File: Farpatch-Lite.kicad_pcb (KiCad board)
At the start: 2 copper layers, 34 x 12.2 mm, 33 parts, among them J1 Program Header, J2 SWD Connector, SW1 Pushbutton 2.1x1.6mm, SW2 Pushbutton 2.1x1.6mm, U1 ‎ESP32-D0WD-V3‎, U2 Flash 32 Mb SPI, Y1 Crystal 40MHz

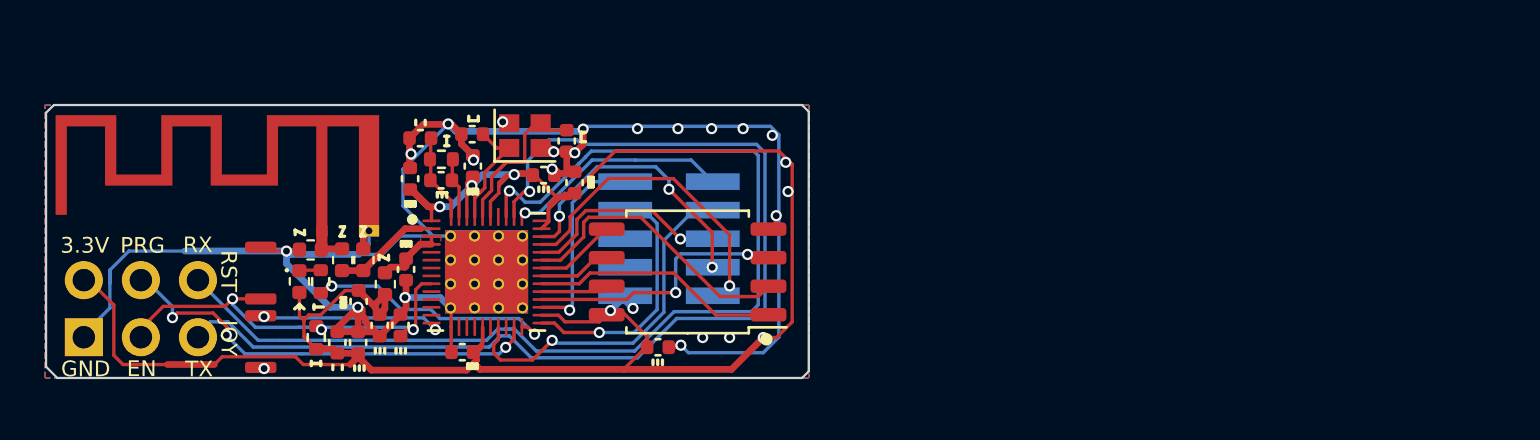
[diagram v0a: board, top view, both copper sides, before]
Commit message: farpatch-lite: Add fabrication data to PCB
Signed-off-by: Sean Cross <sean@xobs.io>
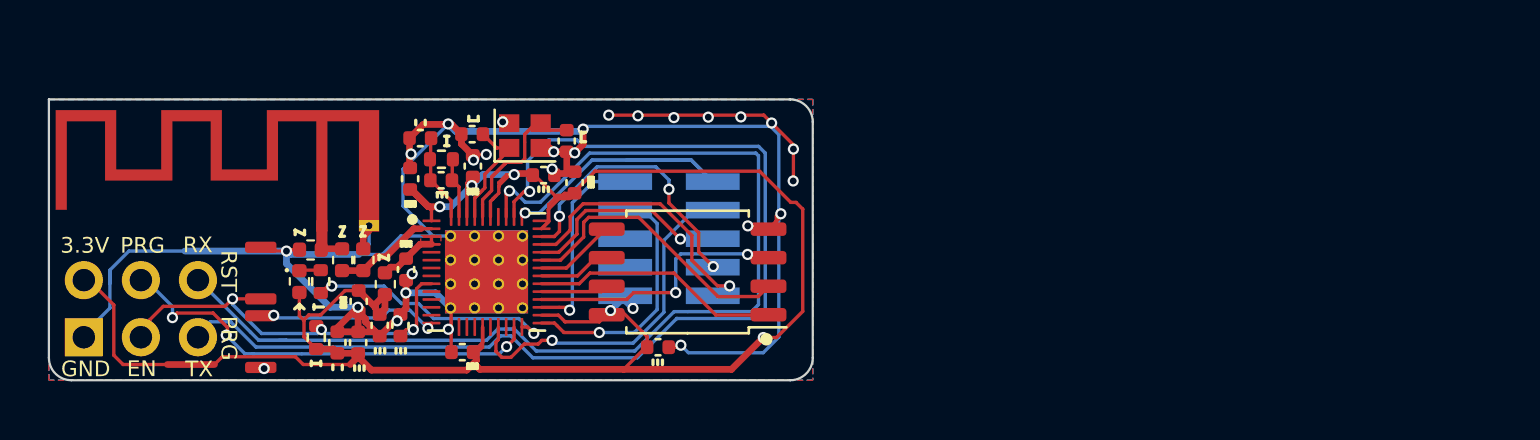
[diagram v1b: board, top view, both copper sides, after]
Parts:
- moved A1 0.22 mm to (86.7, 104.6)
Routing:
- net GND: track 86.9 -> 98.8 mm, vias 23 -> 27
- net /TGT_RESET: track 9.96 -> 18.6 mm
- net /TGT_SWDIO: track 13.9 -> 12.3 mm
- net V3V3: track 98.6 -> 97.3 mm
- net /UART_TX: track 48.0 -> 49.1 mm
- net /EN: track 18.5 -> 17.7 mm
- net Net-(SW1-Pad1): track 8.23 -> 7.69 mm
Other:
- board size 34 x 12.2 mm -> 34 x 12.5 mm
- board text added: "0"
- board text added: "0 mm"
- board text added: "0.01 mm"
- board text added: "0.02"
- board text added: "0.035 mm"
- board text added: "0.1500 mm / 0.0000 mm"
- board text added: "0.3000 mm"
- board text added: "1"
- board text added: "1.51 mm"
- board text added: "1.6000 mm"
- board text added: "2"
- board text added: "3.3"
- board text added: "34.0000 mm x 12.5000 mm"
- board text added: "4.5"
- board text added: "B.Cu"
- board text added: "B.Mask"
- board text added: "B.Paste"
- board text added: "B.Silkscreen"
- board text added: "BOARD CHARACTERISTICS"
- board text added: "Blue"
- board text added: "Board Thickness:"
- board text added: "Board overall dimensions:"
- board text added: "Bottom Silk Screen"
- board text added: "Bottom Solder Mask"
- board text added: "Bottom Solder Paste"
- board text added: "Castellated pads:"
- board text added: "Color"
- board text added: "Copper Finish:"
- board text added: "Copper Layer Count:"
- board text added: "Dielectric"
- board text added: "ENIG"
- board text added: "Edge card connectors:"
- board text added: "Epsilon R"
- board text added: "F.Cu"
- board text added: "F.Mask"
- board text added: "F.Paste"
- board text added: "F.Silkscreen"
- board text added: "FR4"
- board text added: "Farpatch Lite EVT1 (c) 2022 Foosn PTE Ltd"
- board text added: "Impedance Control:"
- board text added: "Layer Name"
- board text added: "Loss Tangent"
- board text added: "Material"
- board text added: "Min hole diameter:"
- board text added: "Min track/spacing:"
- board text added: "No"
- board text added: "Not specified"
- board text added: "Plated Board Edge:"
- board text added: "Thickness (mm)"
- board text added: "Top Silk Screen"
- board text added: "Top Solder Mask"
- board text added: "Top Solder Paste"
- board text added: "Type"
- board text added: "White"
- board text added: "copper"
- board text added: "core"
- board text removed: "JOY"
- board text removed: "Wifi Debug 32 EVT1 (c) 2022 Foosn PTE Ltd"

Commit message: farpatch: finish layout and update README
Signed-off-by: Sean Cross <sean@xobs.io>
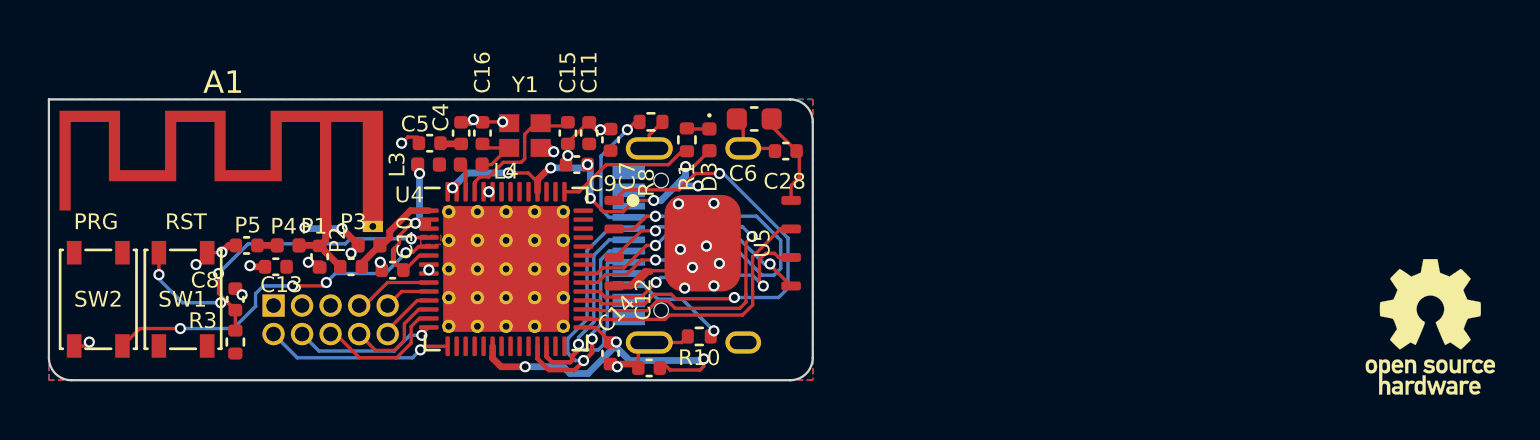
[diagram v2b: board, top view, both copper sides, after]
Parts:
- removed C1, C2: Cap 12pF 0402, Capacitor_SMD:C_0402_1005Metric
- removed C3: Cap 10uF 0402, Capacitor_SMD:C_0402_1005Metric
- removed D1: Red LED, Farpatch-Lite:LED_0402_1005Metric
- removed J1: Program Header, Farpatch-Lite:PinHeader_2x03_P2.54mm_Vertical
- removed L1, L2: Ind 2.2nH 0402, Inductor_SMD:L_0402_1005Metric
- removed R2: Res 20k 0402, Resistor_SMD:R_0402_1005Metric
- removed U1: ‎ESP32-D0WD-V3‎, Farpatch-Lite:QFN-48-1EP_5x5mm_P0.35mm_EP3.7x3.7mm_ThermalVias
- removed U2: Flash 32 Mb SPI, Farpatch-Lite:SOIC-8_5.23x5.23mm_P1.27mm
- added C28: Cap 100nF 0402, Capacitor_SMD:C_0402_1005Metric, F.Cu at (107.3, 101.3)
- added D3: Red LED 0402, Farpatch-Lite:LED_0402_1005Metric, F.Cu at (103.9, 100.8)
- added J3: USB-C Receptacle (USB2.0), Farpatch-Lite:USB_C_Receptacle_HRO_TYPE-C-31-M-12, B.Cu at (104.4, 105.5)
- added LOGO2: Logo_Open_Hardware_Small, Symbol:OSHW-Logo_5.7x6mm_SilkScreen, F.Cu at (136.0, 109.1)
- added P1: Cap 2.4pF 0402, Capacitor_SMD:C_0402_1005Metric, F.Cu at (86.5, 106.0)
- added P2: Cap 3.9pF 0402, Capacitor_SMD:C_0402_1005Metric, F.Cu at (88.0, 106.5)
- added P3: L 2.7 nH 0402, Inductor_SMD:L_0402_1005Metric, F.Cu at (88.8, 105.5)
- added P4: L 2.7 nH 0402, Inductor_SMD:L_0402_1005Metric, F.Cu at (85.2, 105.5)
- added P5: Cap 3.9pF 0402, Capacitor_SMD:C_0402_1005Metric, F.Cu at (83.3, 105.5)
- added R10: R 5.1k 0402, Resistor_SMD:R_0402_1005Metric, F.Cu at (103.5, 109.5)
- added R8: R 5.1k 0402, Resistor_SMD:R_0402_1005Metric, F.Cu at (101.3, 100.0)
- added U4: ESP32-S3, Farpatch-Lite:QFN-56-1EP_7x7mm_P0.4mm_EP5.6x5.6mm_ThermalVias, F.Cu at (94.8, 106.5)
- added U5: Flash 256 Mbit SPI, Farpatch-Lite:WSON-8_8x6mm_P1.27mm, F.Cu at (103.6, 105.4)
- C13, C7: value Cap 100nF 0402 -> Cap 1uF 0402
- C14: value Cap 1uF 0402 -> Cap 100nF 0402
- C15: value Cap 100nF 0402 -> Cap 12pF 0402
- C16: value Cap 1uF 0402 -> Cap 12pF 0402
- C5: value Cap 1uF 0402 -> Cap 10nF 0402
- C6: value Cap 10nF 0402 -> Cap 10uF 0603; footprint Capacitor_SMD:C_0402_1005Metric -> Capacitor_SMD:C_0603_1608Metric
- C9: value Cap 3.3nF 0402 -> Cap 100nF 0402
- J2: footprint Farpatch-Lite:PinHeader_2x05_P1.27mm_Vertical_SMD -> Connector_PinHeader_1.27mm:PinHeader_2x05_P1.27mm_Vertical
- L3: value Ind 2.2nH 0402 -> L 2.2nH 0402
- L4: value Ind 2.2nH 0402 -> L 20nH 0402
- LOGO1: value Logo_Open_Hardware_Large -> Farpatch Logo; footprint Symbol:OSHW-Logo_5.7x6mm_SilkScreen -> Farpatch-Lite:Farpatch Logo
- R1: value Res 20k 0402 -> Res 200 0402
- R3: value Res 200 0402 -> Res 20k 0402
- SW1, SW2: value Pushbutton 2.1x1.6mm -> Pushbutton 4.2x3.2mm 250gf; footprint Farpatch-Lite:Pushbutton-2.1x1.6mm -> Farpatch-Lite:SW_SPST_PTS810
- Y1: value Crystal 40MHz -> Crystal 40MHz 2016
- moved J2 17.8 mm to (84.5, 108.2), turned to -90 degrees
- moved C6 14.9 mm to (105.9, 99.9)
- moved C8 14.8 mm to (82.8, 107.9), turned to 90 degrees
- moved C7 13.3 mm to (99.5, 100.8), turned to 90 degrees
- moved C16 12.3 mm to (93.8, 100.5), turned to 90 degrees
- moved R1 11.0 mm to (102.9, 100.8), turned to 90 degrees
- moved C11 10.2 mm to (98.5, 100.5), turned to 90 degrees
- moved C14 9.43 mm to (99.5, 110.3), turned to -90 degrees
- moved C5 9.43 mm to (91.5, 101.0), turned to 180 degrees
- moved C4 9.29 mm to (92.8, 100.5), turned to 90 degrees
- moved LOGO1 8.59 mm to (82.7, 102.2), turned to 180 degrees
- moved C12 8.35 mm to (101.2, 111.0)
- moved SW2 7.32 mm to (76.7, 107.9), turned to 90 degrees
- moved C13 7.15 mm to (84.6, 106.5), turned to 180 degrees
- moved L4 6.55 mm to (93.3, 101.9), turned to 0 degrees
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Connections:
- C10 pad 1: V3V3 -> /ESP32_VDD3P3
- C11 pad 1: Net-(C11-Pad1) -> VWIFI
- C12 pad 1: V3V3 -> VWIFI
- C13 pad 1: V3V3 -> VWIFI
- C14 pad 1: /EN -> VWIFI
- C15 pad 1: V3V3 -> GND
- C15 pad 2: GND -> Net-(C15-Pad2)
- C16 pad 1: V3V3 -> Net-(C16-Pad1)
- C4 pad 1: V3V3 -> VWIFI
- C5 pad 1: V3V3 -> VWIFI
- C6 pad 1: Net-(C6-Pad1) -> VWIFI
- C7 pad 1: V3V3 -> VWIFI
- C8 pad 1: V3V3 -> /ESP32_EN
- C9 pad 1: Net-(C9-Pad1) -> VWIFI
- C9 pad 2: Net-(C6-Pad1) -> GND
- J2 pad 1: V3V3 -> VWIFI
- J2 pad 10: /TGT_RESET -> /NRESET
- J2 pad 2: /TGT_SWDIO -> /SWDIO/TMS
- J2 pad 4: /TGT_SWCLK -> /SWCLK/TCK
- J2 pad 6: /TGT_SWO -> /SWO/TDO
- J2 pad 7: /TGT_UART_TX -> /UART_UTX
- J2 pad 8: /TGT_TDI -> /TDI
- J2 pad 9: /TGT_UART_RX -> /UART_URX
- L3 pad 1: GND -> VWIFI
- L3 pad 2: Net-(L2-Pad2) -> /ESP32_VDD3P3
- L4 pad 1: V3V3 -> Net-(L4-Pad1)
- L4 pad 2: Net-(C11-Pad1) -> Net-(C16-Pad1)
- R1 pad 1: Net-(C6-Pad1) -> /LED1_CTRL
- R1 pad 2: Net-(C9-Pad1) -> Net-(D3-Pad1)
- R3 pad 1: Net-(R3-Pad1) -> /ESP32_EN
- R3 pad 2: Net-(D1-Pad1) -> VWIFI
- SW1 pad 1: Net-(SW1-Pad1) -> GND
- SW1 pad 2: GND -> /ESP32_EN
- SW2 pad 2: /EN -> /BOOT_MODE
- Y1 pad 1: Net-(C2-Pad1) -> Net-(C16-Pad1)
- Y1 pad 3: Net-(C1-Pad2) -> Net-(C15-Pad2)
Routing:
- net V3V3: track 97.3 -> 0.00 mm, vias 6 -> 0
- net GND: track 98.8 -> 28.2 mm
- net /UART_TX: track 49.1 -> 0.00 mm, vias 1 -> 0
- net /UART_RX: track 48.5 -> 0.00 mm, vias 1 -> 0
- net VWIFI: track 0.00 -> 37.2 mm, vias 0 -> 11
- net /SPI_CS: track 0.00 -> 21.3 mm, vias 0 -> 2
- net /SPI_IO1: track 0.00 -> 19.2 mm, vias 0 -> 2
- net /TGT_RESET: track 18.6 -> 0.00 mm, vias 1 -> 0
- net /ESP32_EN: track 0.00 -> 18.0 mm, vias 0 -> 4
- net /EN: track 17.7 -> 0.00 mm, vias 3 -> 0
- net /SPI_IO2: track 0.00 -> 17.6 mm, vias 0 -> 2
- net /USB_DN: track 0.00 -> 17.2 mm, vias 0 -> 2
- net /USB_DP: track 0.00 -> 14.9 mm, vias 0 -> 1
- net /TGT_TDI: track 14.8 -> 0.00 mm, vias 1 -> 0
- net Net-(U1-Pad33): track 12.9 -> 0.00 mm
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- added copper zone on F.Cu, net Net-(C16-Pad1)
- added copper zone on B.Cu, net VWIFI
- added copper zone on F.Cu, net VWIFI
- removed copper zone on F.Cu, net Net-(C11-Pad1)
- removed copper zone on B.Cu, net V3V3
- removed copper zone on F.Cu, net V3V3
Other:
- board text added: "08/2022"
- board text added: "Designed in Singapore"
- board text removed: "01/2022"
- board text removed: "3.3V"
- board text removed: "Designed in SG"
- board text removed: "EN"
- board text removed: "GND"
- board text removed: "RX"
- board text removed: "TX"

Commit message: evt1: switch to 4-layer PCB
While it's possible to route the board in two layers, four layers
are more reliable.

Signed-off-by: Sean Cross <sean@xobs.io>
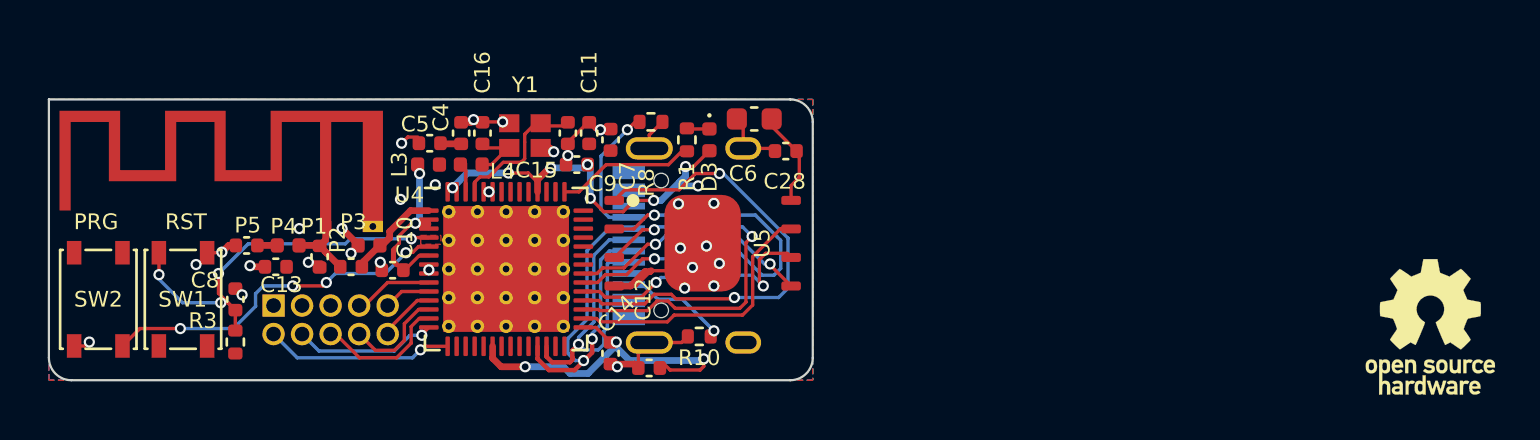
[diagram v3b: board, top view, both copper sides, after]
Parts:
- moved LOGO1 1.42 mm to (82.5, 103.5), turned to 90 degrees
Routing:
- net GND: track 28.2 -> 26.6 mm, vias 27 -> 28
- net VWIFI: vias 11 -> 12
- added copper zone on In1.Cu, net GND
- added copper zone on In2.Cu, net VWIFI
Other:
- copper layers 2 -> 4
- board text added: "Only use with 3.3V targets!"
